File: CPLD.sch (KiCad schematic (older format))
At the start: 46 parts, among them J2 JTAG, Q1 IRLML6402, Q2 IRLML6402, U2 EPM7064STC100, X1 CFPS-72 50mhz

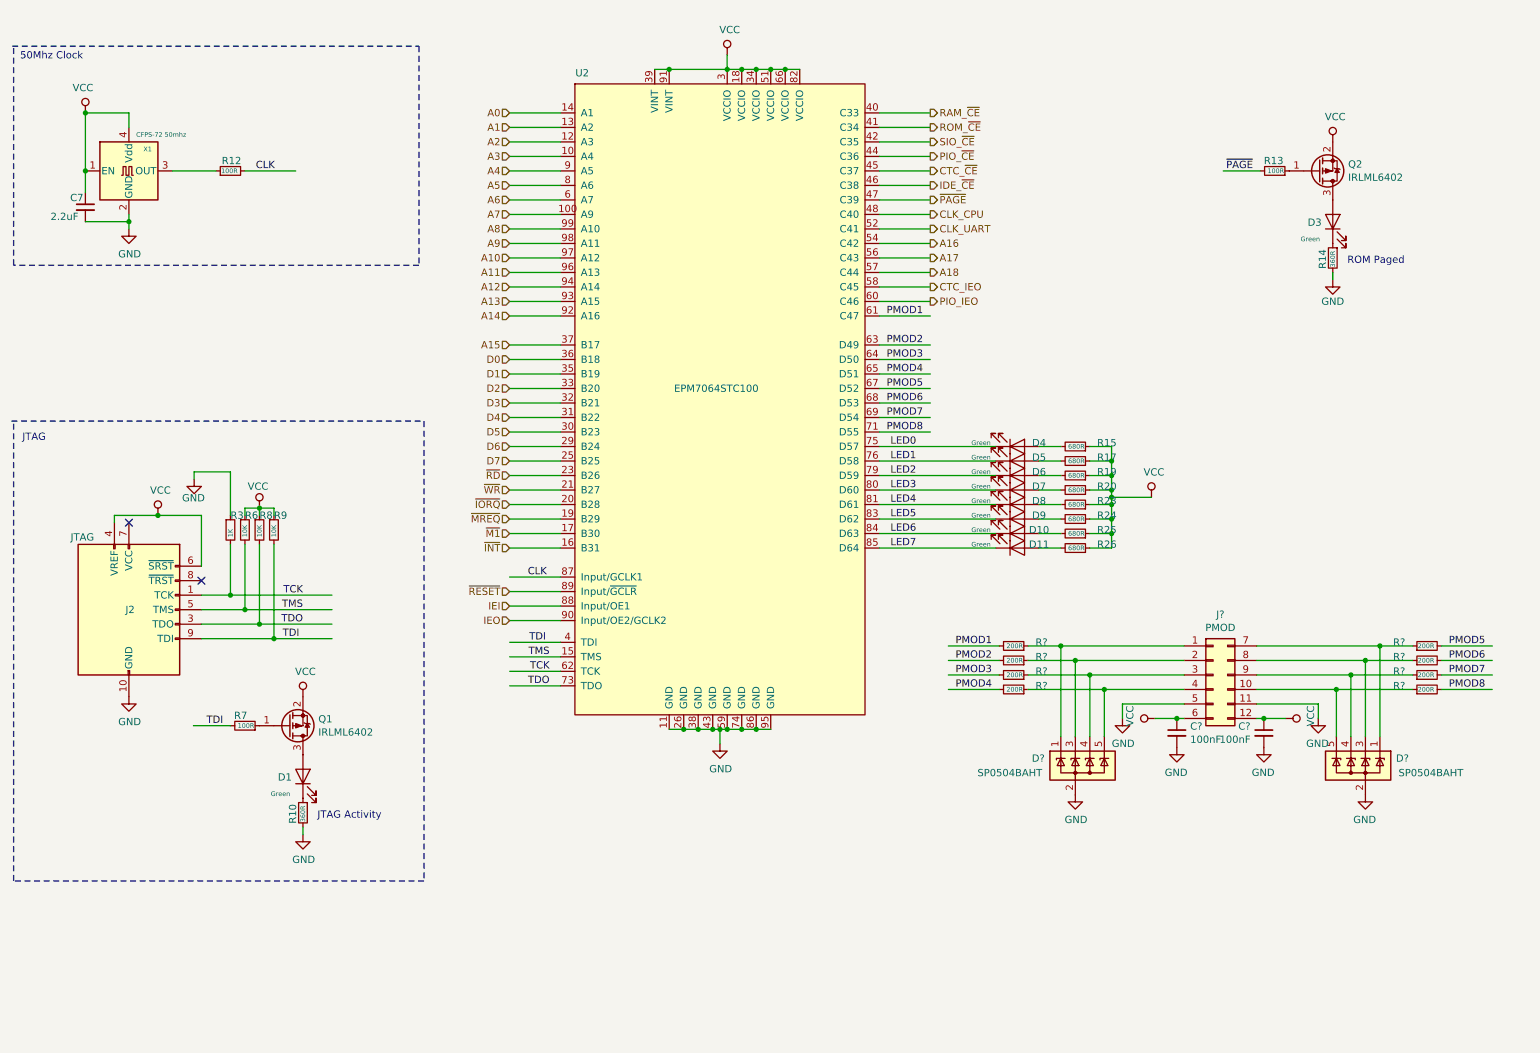
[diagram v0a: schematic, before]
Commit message: reset annotations, added dip switch
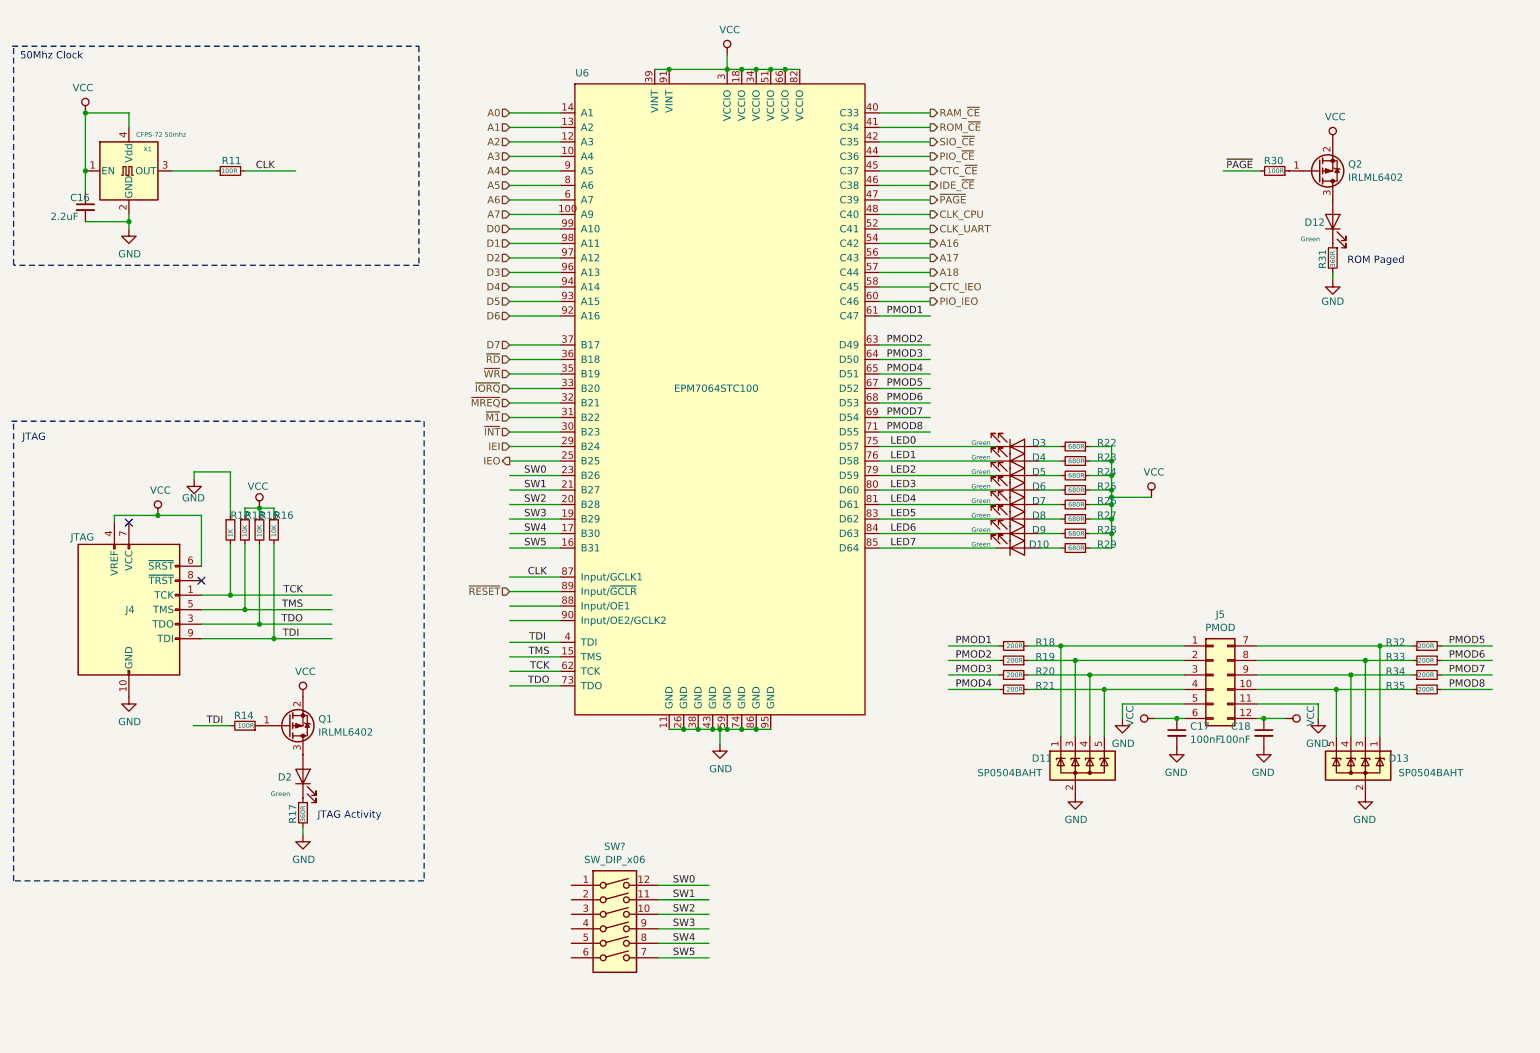
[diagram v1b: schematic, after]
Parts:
- added SW?: SW_DIP_x06, symbol Switch:SW_DIP_x06
- gave numbers to parts that had none: 13
- renumbered C7 to C16, D11 to D10, D3 to D12, D1 to D2, D4 to D3, D5 to D4, D6 to D5, D7 to D6, D8 to D7, D9 to D8, D10 to D9, J2 to J4, R12 to R11, R3 to R12, R6 to R13, R7 to R14, R8 to R15, R9 to R16, R10 to R17, R15 to R22, R17 to R23, R19 to R24, R20 to R25, R23 to R26, R24 to R27, R25 to R28, R26 to R29, R13 to R30, R14 to R31, U2 to U6
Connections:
- net labels added: SW0, SW1, SW2, SW3, SW4, SW5
- net labels removed: A10, A11, A12, A13, A14, A15, A8, A9
- wire segments 187 -> 193

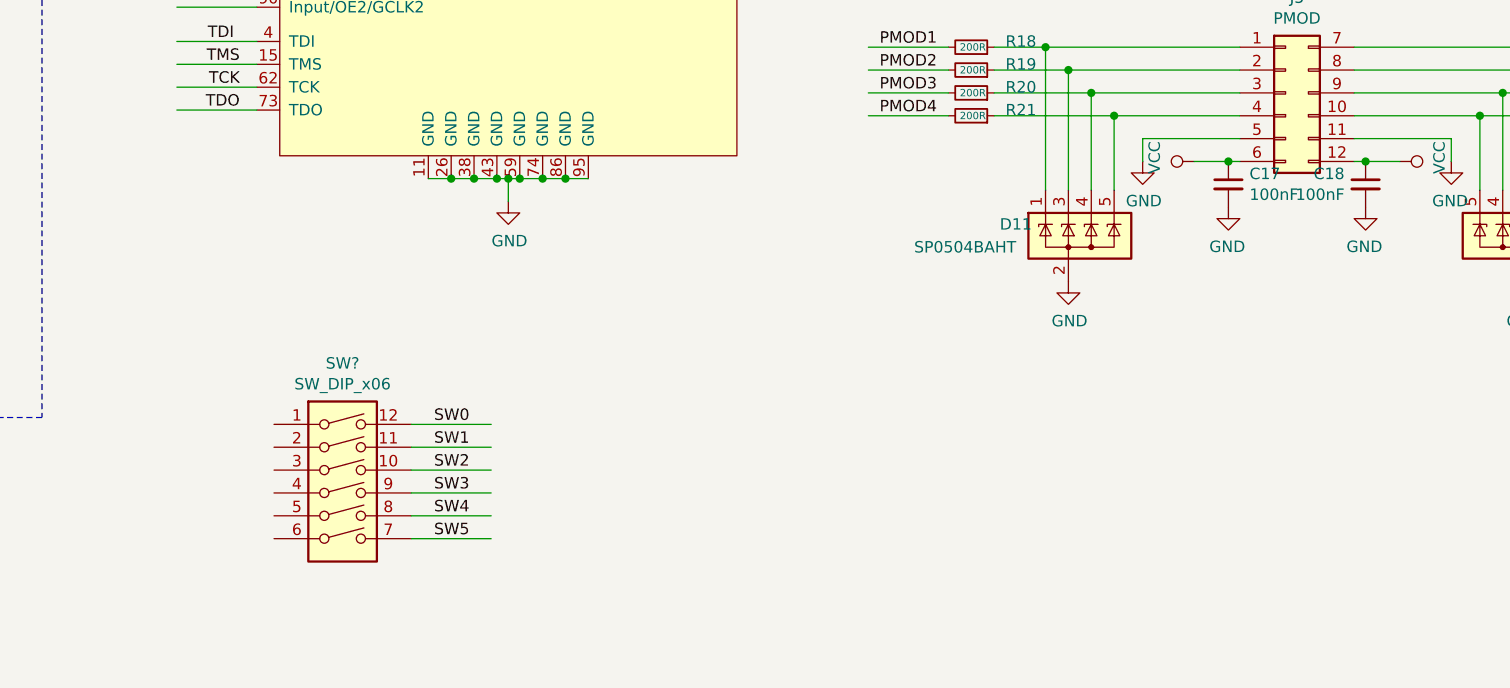
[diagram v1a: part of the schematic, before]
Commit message: added switch pullups
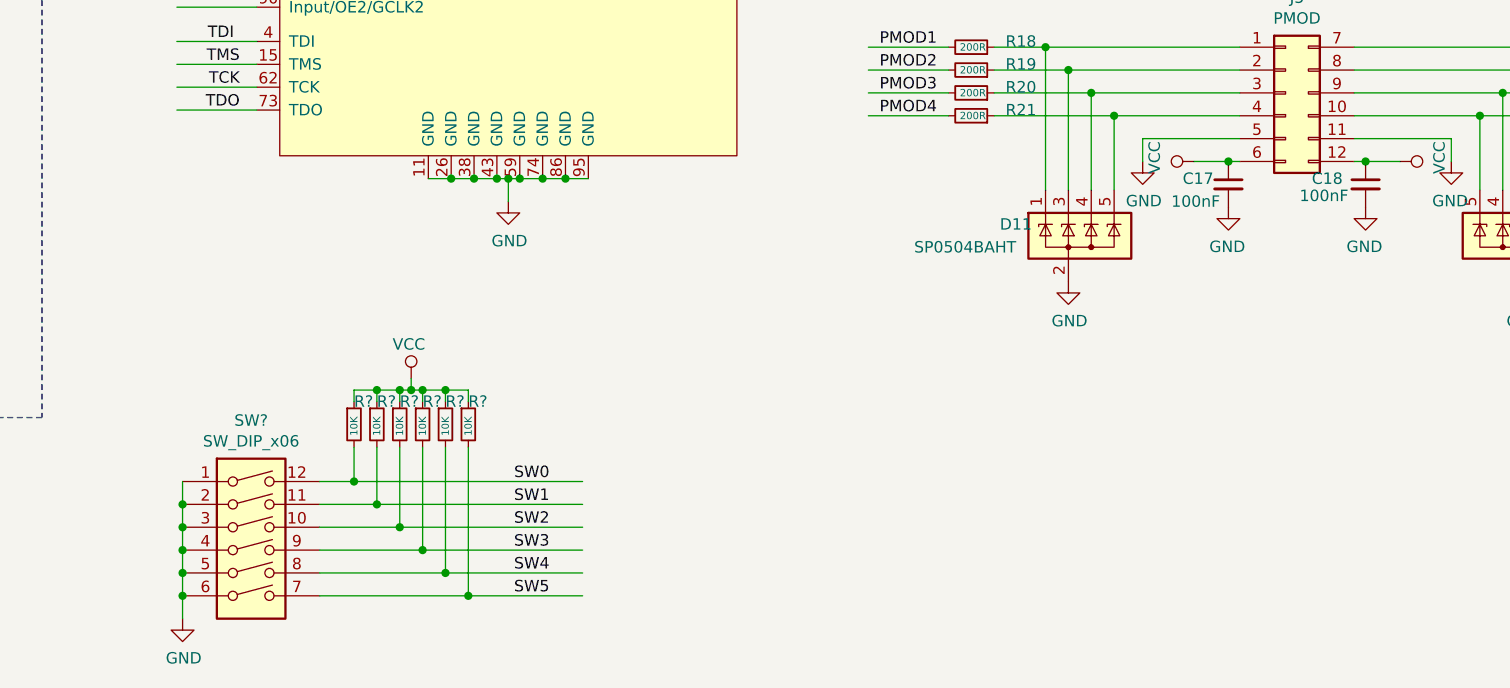
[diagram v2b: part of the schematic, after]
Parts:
- added R? (x6): 10K, Resistor_SMD:R_0603_1608Metric_Pad1.05x0.95mm_HandSolder, symbol Device:R_Small
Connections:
- wire segments 193 -> 224
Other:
- moved on the sheet: SW?

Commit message: regridded
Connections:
- net labels added: PMOD0
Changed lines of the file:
@@
 Text HLabel 6875 2425 2    50   Output ~ 0
 PIO_IEO
-Text Label 6825 2525 2    50   ~ 0
+Text Label 6800 2725 2    50   ~ 0
 PMOD1
-Text Label 6825 2725 2    50   ~ 0
+Text Label 6800 2825 2    50   ~ 0
 PMOD2
-Text Label 6825 2825 2    50   ~ 0
+Text Label 6800 2925 2    50   ~ 0
 PMOD3
-Text Label 6825 2925 2    50   ~ 0
+Text Label 6800 3025 2    50   ~ 0
 PMOD4
-Text Label 6825 3025 2    50   ~ 0
+Text Label 6800 3125 2    50   ~ 0
 PMOD5
-Text Label 6825 3125 2    50   ~ 0
+Text Label 6800 3225 2    50   ~ 0
 PMOD6
-Text Label 6825 3225 2    50   ~ 0
+Text Label 6800 3325 2    50   ~ 0
 PMOD7
-Text Label 6825 3325 2    50   ~ 0
-PMOD8
 Wire Wire Line
 	7350 4800 7000 4800
@@
 	7350 5100 7000 5100
 Text Label 7300 4800 2    50   ~ 0
+PMOD0
+Text Label 7300 4900 2    50   ~ 0
 PMOD1
-Text Label 7300 4900 2    50   ~ 0
+Text Label 7300 5000 2    50   ~ 0
 PMOD2
-Text Label 7300 5000 2    50   ~ 0
+Text Label 7300 5100 2    50   ~ 0
 PMOD3
-Text Label 7300 5100 2    50   ~ 0
-PMOD4
 $Comp
 L Device:R_Small R?
@@
 	10400 5100 10750 5100
 Text Label 10450 4800 0    50   ~ 0
+PMOD4
+Text Label 10450 4900 0    50   ~ 0
 PMOD5
-Text Label 10450 4900 0    50   ~ 0
-PMOD6
 Text Label 10450 5000 0    50   ~ 0
 PMOD7
@@
 	1    0    0    -1
 $EndComp
+Text Label 6800 2525 2    50   ~ 0
+PMOD0
 $EndSCHEMATC

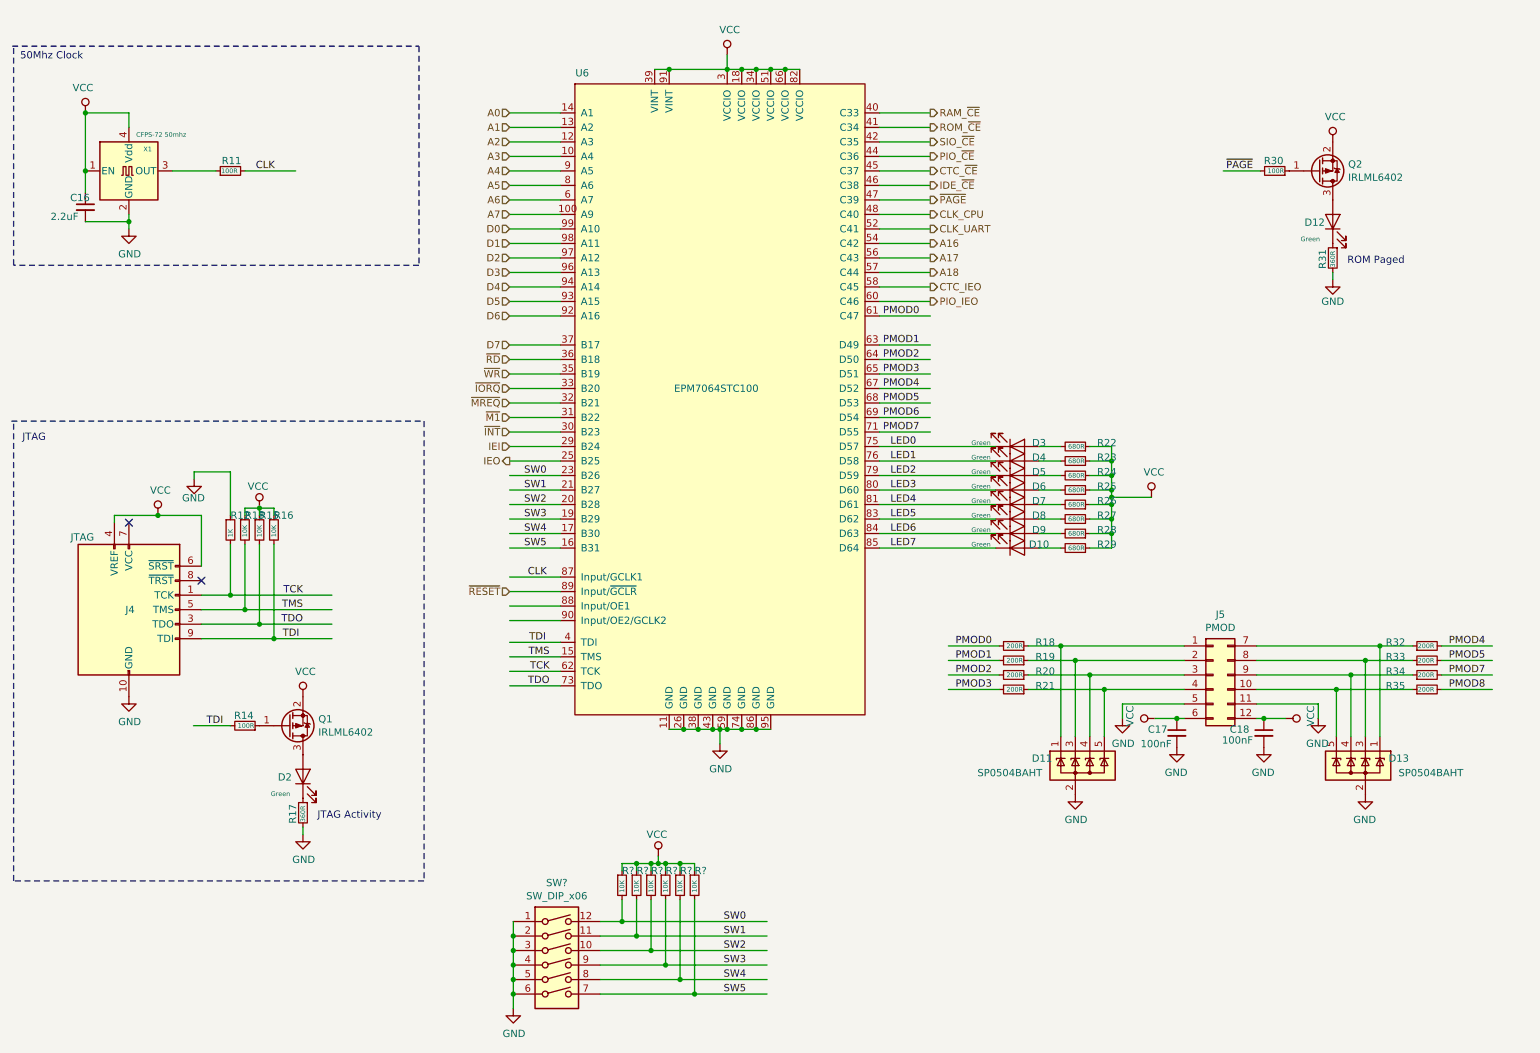
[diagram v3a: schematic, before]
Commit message: connect sheet pins
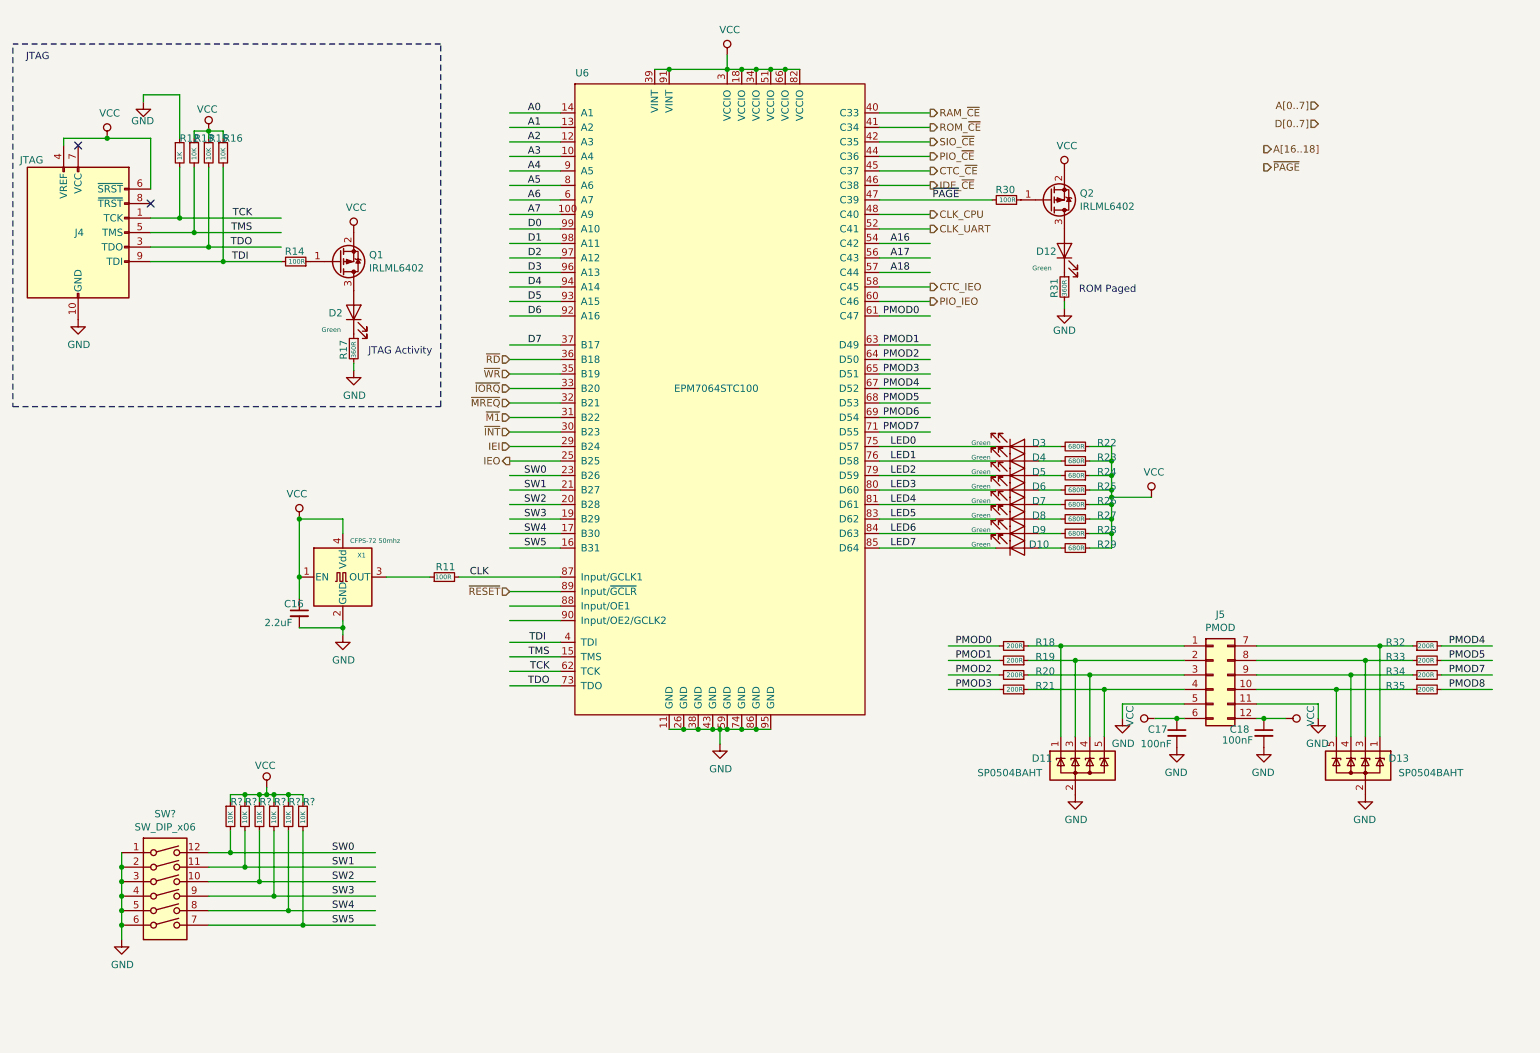
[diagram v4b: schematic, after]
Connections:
- net labels added: A[0..7], A[16..18], D[0..7]
- wire segments 224 -> 221
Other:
- note removed: "50Mhz Clock"
- moved on the sheet: C16, D12, D2, J4, Q1, Q2, R11, R12, R13, R14, R15, R16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
